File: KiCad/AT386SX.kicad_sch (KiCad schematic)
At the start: 35 parts, among them J13 Front Panel, J14 CPU 1-25, J15 CPU 26-50, J16 CPU 51-75, J17 CPU 76-100, Q1 2N3904, SW1 Power, SW2 Reset, U1 80386SX, U2 80387SX, U3 RC2016A5, U7 74HC05, X1 CPU_CLK, X2 FPU_CLK, Y1 14.31818MHz

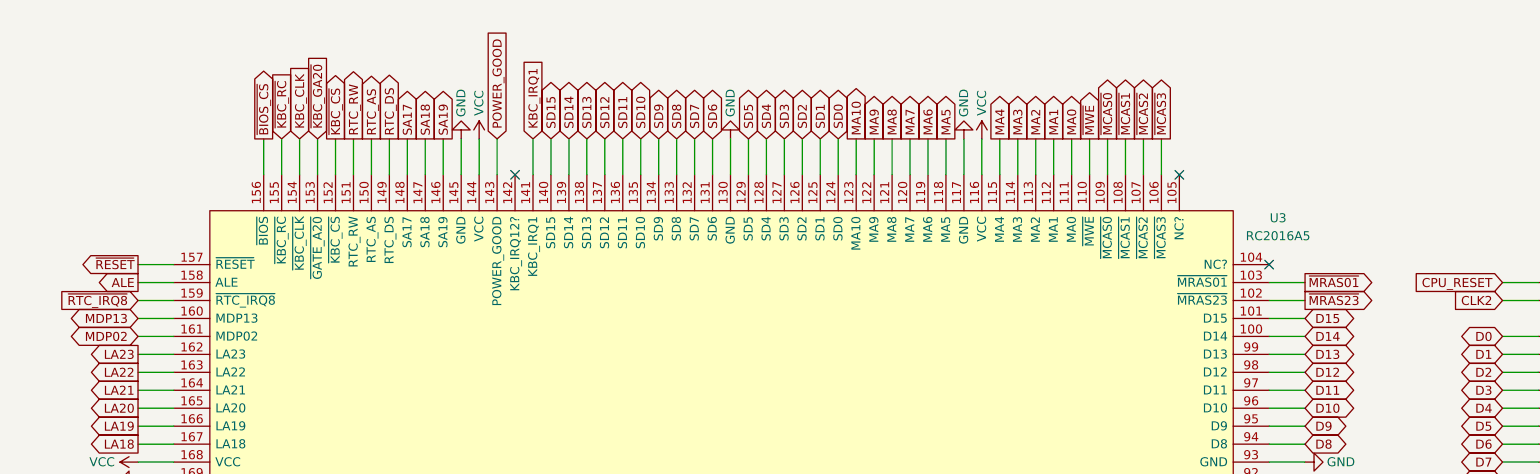
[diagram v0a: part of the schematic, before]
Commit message: Fix the ROM /OE issue; Update DRAM banks
Connect Flash ROM /OE to ISA /MEMR
Update DRAM banks numbers (swap Bank 0 and Bank 1)
Update chipset DRAM signal names
Renumber DRAM termination resistors according to the signal names
Renumber SIMM and ISA slots, so that they are numbered top to bottom
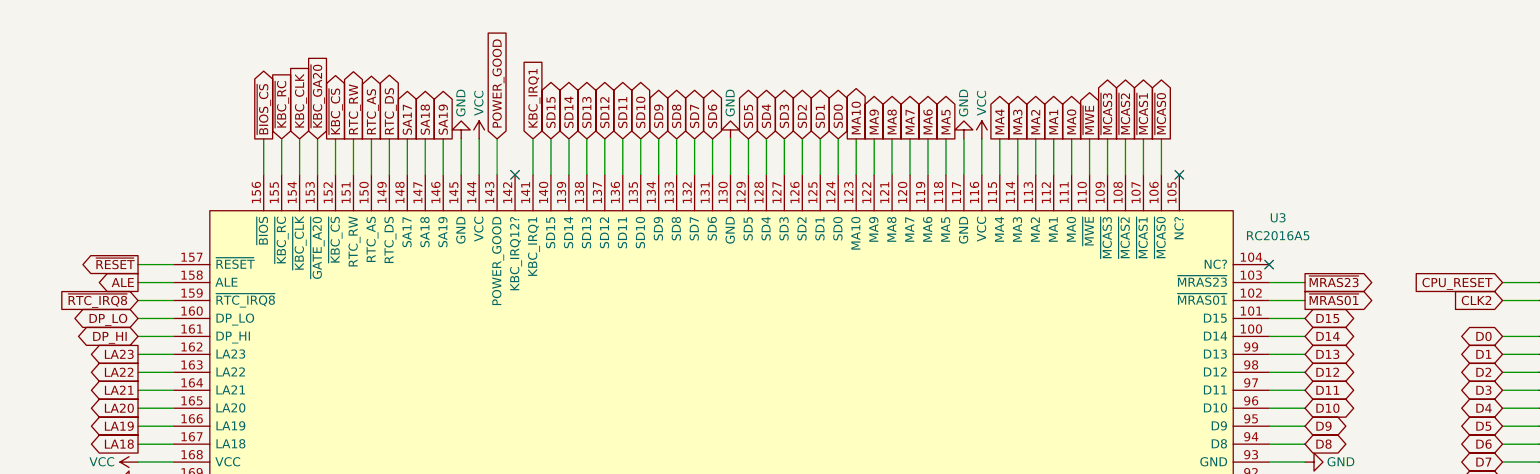
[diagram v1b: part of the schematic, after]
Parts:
- U3: footprint My_Components:PQFP-208_28x28mm_P0.5mm_Handsoldering -> Package_QFP:PQFP-208_28x28mm_P0.5mm
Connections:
- net ~{MCAS0}: now also U3.106 (~{MCAS0}); no longer U3.109 (~{MCAS0})
- net ~{MCAS1}: now also U3.107 (~{MCAS1}); no longer U3.108 (~{MCAS1})
- net ~{MCAS2}: now also U3.108 (~{MCAS2}); no longer U3.107 (~{MCAS2})
- net ~{MCAS3}: now also U3.109 (~{MCAS3}); no longer U3.106 (~{MCAS3})
- net ~{MRAS01}: now also U3.102 (~{MRAS01}); no longer U3.103 (~{MRAS01})
- net ~{MRAS23}: now also U3.103 (~{MRAS23}); no longer U3.102 (~{MRAS23})
- net MDP02 renamed DP_HI
- net MDP13 renamed DP_LO
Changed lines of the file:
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@@
   (title_block
     (title "386SX Motherboard Based on SARC RC2016 Chipset")
-    (date "2026-01-28")
-    (rev "2.1")
+    (date "2026-02-17")
+    (rev "2.2")
     (company "Copyright (C) 2024-2026 Sergey Kiselev")
     (comment 1 "https://github.com/Marco-Both/M396F-Replika")
@@
     )
   )
-  (global_label "MDP02" (shape tri_state) (at 25.4 58.42 180) (fields_autoplaced)
+  (global_label "DP_HI" (shape tri_state) (at 25.4 58.42 180) (fields_autoplaced)
     (effects (font (size 1.27 1.27)) (justify right))
-    (property "Intersheet References" "${INTERSHEET_REFS}" (id 0) (at 16.5764 58.3406 0)
+    (property "Intersheet References" "${INTERSHEET_REFS}" (id 0) (at 17.544 58.3406 0)
       (effects (font (size 1.27 1.27)) (justify right) hide)
     )
   )
-  (global_label "~{MCAS1}" (shape output) (at 165.1 30.48 90) (fields_autoplaced)
+  (global_label "~{MCAS2}" (shape output) (at 165.1 30.48 90) (fields_autoplaced)
     (effects (font (size 1.27 1.27)) (justify left))
     (property "Intersheet References" "${INTERSHEET_REFS}" (id 0) (at 165.0206 21.8379 90)
@@
     )
   )
-  (global_label "MDP13" (shape tri_state) (at 25.4 55.88 180) (fields_autoplaced)
+  (global_label "DP_LO" (shape tri_state) (at 25.4 55.88 180) (fields_autoplaced)
     (effects (font (size 1.27 1.27)) (justify right))
-    (property "Intersheet References" "${INTERSHEET_REFS}" (id 0) (at 16.5764 55.8006 0)
+    (property "Intersheet References" "${INTERSHEET_REFS}" (id 0) (at 17.1207 55.8006 0)
       (effects (font (size 1.27 1.27)) (justify right) hide)
     )
@@
     )
   )
-  (global_label "~{MCAS3}" (shape output) (at 170.18 30.48 90) (fields_autoplaced)
+  (global_label "~{MCAS0}" (shape output) (at 170.18 30.48 90) (fields_autoplaced)
     (effects (font (size 1.27 1.27)) (justify left))
     (property "Intersheet References" "${INTERSHEET_REFS}" (id 0) (at 170.1006 21.8379 90)
@@
     )
   )
-  (global_label "~{MCAS2}" (shape output) (at 167.64 30.48 90) (fields_autoplaced)
+  (global_label "~{MCAS1}" (shape output) (at 167.64 30.48 90) (fields_autoplaced)
     (effects (font (size 1.27 1.27)) (justify left))
     (property "Intersheet References" "${INTERSHEET_REFS}" (id 0) (at 167.5606 21.8379 90)
@@
     )
   )
-  (global_label "~{MRAS23}" (shape output) (at 190.5 53.34 0) (fields_autoplaced)
+  (global_label "~{MRAS01}" (shape output) (at 190.5 53.34 0) (fields_autoplaced)
     (effects (font (size 1.27 1.27)) (justify left))
     (property "Intersheet References" "${INTERSHEET_REFS}" (id 0) (at 200.3517 53.2606 0)
@@
     )
   )
-  (global_label "~{MRAS01}" (shape output) (at 190.5 50.8 0) (fields_autoplaced)
+  (global_label "~{MRAS23}" (shape output) (at 190.5 50.8 0) (fields_autoplaced)
     (effects (font (size 1.27 1.27)) (justify left))
     (property "Intersheet References" "${INTERSHEET_REFS}" (id 0) (at 200.3517 50.7206 0)
@@
     )
   )
-  (global_label "~{MCAS0}" (shape output) (at 162.56 30.48 90) (fields_autoplaced)
+  (global_label "~{MCAS3}" (shape output) (at 162.56 30.48 90) (fields_autoplaced)
     (effects (font (size 1.27 1.27)) (justify left))
     (property "Intersheet References" "${INTERSHEET_REFS}" (id 0) (at 162.4806 21.8379 90)
@@
     (property "Reference" "U3" (id 0) (at 186.69 41.6812 0))
     (property "Value" "RC2016A5" (id 1) (at 186.69 44.2212 0))
-    (property "Footprint" "My_Components:PQFP-208_28x28mm_P0.5mm_Handsoldering" (id 2) (at 107.95 120.65 0)
+    (property "Footprint" "Package_QFP:PQFP-208_28x28mm_P0.5mm" (id 2) (at 107.95 120.65 0)
       (effects (font (size 1.27 1.27)) hide)
     )
@@
       (reference "H7") (unit 1) (value "HOLE") (footprint "MountingHole:MountingHole_4mm_Pad_Via")
     )
-    (path "/b540f997-cabb-4061-85a0-370b4e9dd03a/520377df-283d-4c0c-a508-48b0439a5c71"
-      (reference "J1") (unit 1) (value "BUSAT_HOST") (footprint "My_Components:Conn_Edge_ISA16")
+    (path "/1c0f074e-275c-4c09-93e3-0959df27fb02/069056e6-b6c0-4250-b4d3-e0552f9a5620"
+      (reference "J1") (unit 1) (value "BANK0") (footprint "My_Components:Conn_SIMM30")
     )
-    (path "/b540f997-cabb-4061-85a0-370b4e9dd03a/51eb62df-0056-4076-9c17-e8a150c186d7"
-      (reference "J2") (unit 1) (value "BUSAT_HOST") (footprint "My_Components:Conn_Edge_ISA16")
+    (path "/1c0f074e-275c-4c09-93e3-0959df27fb02/0bfae472-811c-4887-9df9-78a9ee9a7876"
+      (reference "J2") (unit 1) (value "BANK0") (footprint "My_Components:Conn_SIMM30")
     )
-    (path "/b540f997-cabb-4061-85a0-370b4e9dd03a/3981a1bc-70ed-4714-964a-8a90eba30fe9"
-      (reference "J3") (unit 1) (value "BUSAT_HOST") (footprint "My_Components:Conn_Edge_ISA16")
+    (path "/1c0f074e-275c-4c09-93e3-0959df27fb02/a2af9dba-42df-4812-8663-360a4f93771d"
+      (reference "J3") (unit 1) (value "BANK1") (footprint "My_Components:Conn_SIMM30")
     )
-    (path "/b540f997-cabb-4061-85a0-370b4e9dd03a/0eedbcbf-cde6-420c-a579-5d2c5bc29faf"
-      (reference "J4") (unit 1) (value "BUSAT_HOST") (footprint "My_Components:Conn_Edge_ISA16")
+    (path "/1c0f074e-275c-4c09-93e3-0959df27fb02/937700a1-26dd-490c-ae66-0b7e3939b8e2"
+      (reference "J4") (unit 1) (value "BANK1") (footprint "My_Components:Conn_SIMM30")
     )
     (path "/b540f997-cabb-4061-85a0-370b4e9dd03a/81311a36-68a4-4fc6-98ca-325f852393c8"
@@
       (reference "J6") (unit 1) (value "BUSAT_HOST") (footprint "My_Components:Conn_Edge_ISA16")
     )
-    (path "/1c0f074e-275c-4c09-93e3-0959df27fb02/937700a1-26dd-490c-ae66-0b7e3939b8e2"
-      (reference "J7") (unit 1) (value "BANK0") (footprint "My_Components:Conn_SIMM30")
+    (path "/b540f997-cabb-4061-85a0-370b4e9dd03a/0eedbcbf-cde6-420c-a579-5d2c5bc29faf"
+      (reference "J7") (unit 1) (value "BUSAT_HOST") (footprint "My_Components:Conn_Edge_ISA16")
     )
-    (path "/1c0f074e-275c-4c09-93e3-0959df27fb02/a2af9dba-42df-4812-8663-360a4f93771d"
-      (reference "J8") (unit 1) (value "BANK0") (footprint "My_Components:Conn_SIMM30")
+    (path "/b540f997-cabb-4061-85a0-370b4e9dd03a/3981a1bc-70ed-4714-964a-8a90eba30fe9"
+      (reference "J8") (unit 1) (value "BUSAT_HOST") (footprint "My_Components:Conn_Edge_ISA16")
     )
-    (path "/1c0f074e-275c-4c09-93e3-0959df27fb02/0bfae472-811c-4887-9df9-78a9ee9a7876"
-      (reference "J9") (unit 1) (value "BANK1") (footprint "My_Components:Conn_SIMM30")
+    (path "/b540f997-cabb-4061-85a0-370b4e9dd03a/51eb62df-0056-4076-9c17-e8a150c186d7"
+      (reference "J9") (unit 1) (value "BUSAT_HOST") (footprint "My_Components:Conn_Edge_ISA16")
     )
-    (path "/1c0f074e-275c-4c09-93e3-0959df27fb02/069056e6-b6c0-4250-b4d3-e0552f9a5620"
-      (reference "J10") (unit 1) (value "BANK1") (footprint "My_Components:Conn_SIMM30")
+    (path "/b540f997-cabb-4061-85a0-370b4e9dd03a/520377df-283d-4c0c-a508-48b0439a5c71"
+      (reference "J10") (unit 1) (value "BUSAT_HOST") (footprint "My_Components:Conn_Edge_ISA16")
     )
     (path "/1c0f074e-275c-4c09-93e3-0959df27fb02/479e2ec2-9712-4822-9c99-fe7c38372dd6"
@@
       (reference "R15") (unit 1) (value "22") (footprint "My_Components:Res_762")
     )
-    (path "/1c0f074e-275c-4c09-93e3-0959df27fb02/71aada45-7808-4276-b161-61d7db249a8f"
+    (path "/1c0f074e-275c-4c09-93e3-0959df27fb02/8ada6564-4809-42ed-8975-d5ba2059e9ee"
       (reference "R16") (unit 1) (value "56") (footprint "My_Components:Res_762")
     )
-    (path "/1c0f074e-275c-4c09-93e3-0959df27fb02/8ada6564-4809-42ed-8975-d5ba2059e9ee"
+    (path "/1c0f074e-275c-4c09-93e3-0959df27fb02/71aada45-7808-4276-b161-61d7db249a8f"
       (reference "R17") (unit 1) (value "56") (footprint "My_Components:Res_762")
     )
-    (path "/1c0f074e-275c-4c09-93e3-0959df27fb02/1dd83d56-3829-4b25-a49a-e029418875da"
+    (path "/1c0f074e-275c-4c09-93e3-0959df27fb02/ba9009d0-5b4b-47a7-9213-8d97184c39f9"
       (reference "R18") (unit 1) (value "100") (footprint "My_Components:Res_762")
     )
-    (path "/1c0f074e-275c-4c09-93e3-0959df27fb02/27df7921-2a79-4c62-aba6-aa28755bddb3"
+    (path "/1c0f074e-275c-4c09-93e3-0959df27fb02/45bd49e3-d781-4dd1-804c-f91d3d2edc7e"
       (reference "R19") (unit 1) (value "100") (footprint "My_Components:Res_762")
     )
-    (path "/1c0f074e-275c-4c09-93e3-0959df27fb02/45bd49e3-d781-4dd1-804c-f91d3d2edc7e"
+    (path "/1c0f074e-275c-4c09-93e3-0959df27fb02/27df7921-2a79-4c62-aba6-aa28755bddb3"
       (reference "R20") (unit 1) (value "100") (footprint "My_Components:Res_762")
     )
-    (path "/1c0f074e-275c-4c09-93e3-0959df27fb02/ba9009d0-5b4b-47a7-9213-8d97184c39f9"
+    (path "/1c0f074e-275c-4c09-93e3-0959df27fb02/1dd83d56-3829-4b25-a49a-e029418875da"
       (reference "R21") (unit 1) (value "100") (footprint "My_Components:Res_762")
     )
@@
     )
     (path "/896c5823-aa74-459b-aeca-0ad46e6df6a4"
-      (reference "U3") (unit 1) (value "RC2016A5") (footprint "My_Components:PQFP-208_28x28mm_P0.5mm_Handsoldering")
+      (reference "U3") (unit 1) (value "RC2016A5") (footprint "Package_QFP:PQFP-208_28x28mm_P0.5mm")
     )
     (path "/1c0f074e-275c-4c09-93e3-0959df27fb02/64fa0391-92f4-4c4f-8a2b-5ba1cb50c4aa"
